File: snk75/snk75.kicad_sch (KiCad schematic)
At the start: 19 parts, among them J1 USB_C_Receptacle_USB2.0, U1 ATmega32U4-AU, Y1 16MHZ

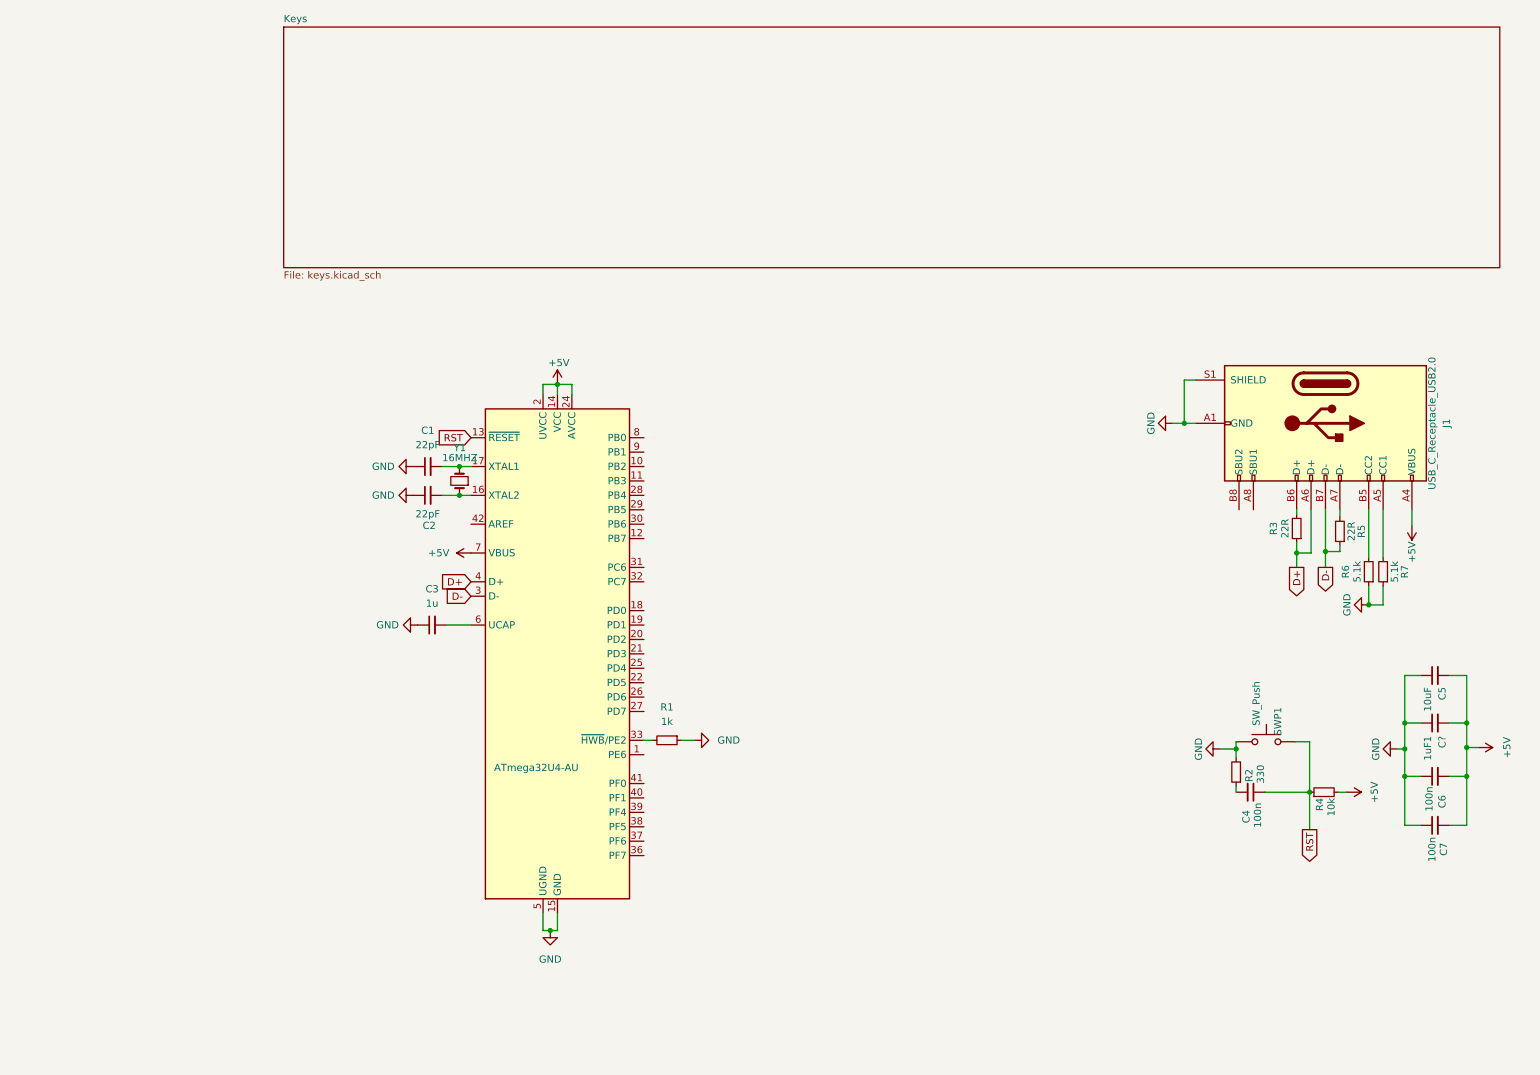
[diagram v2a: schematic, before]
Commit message: Fixed reset
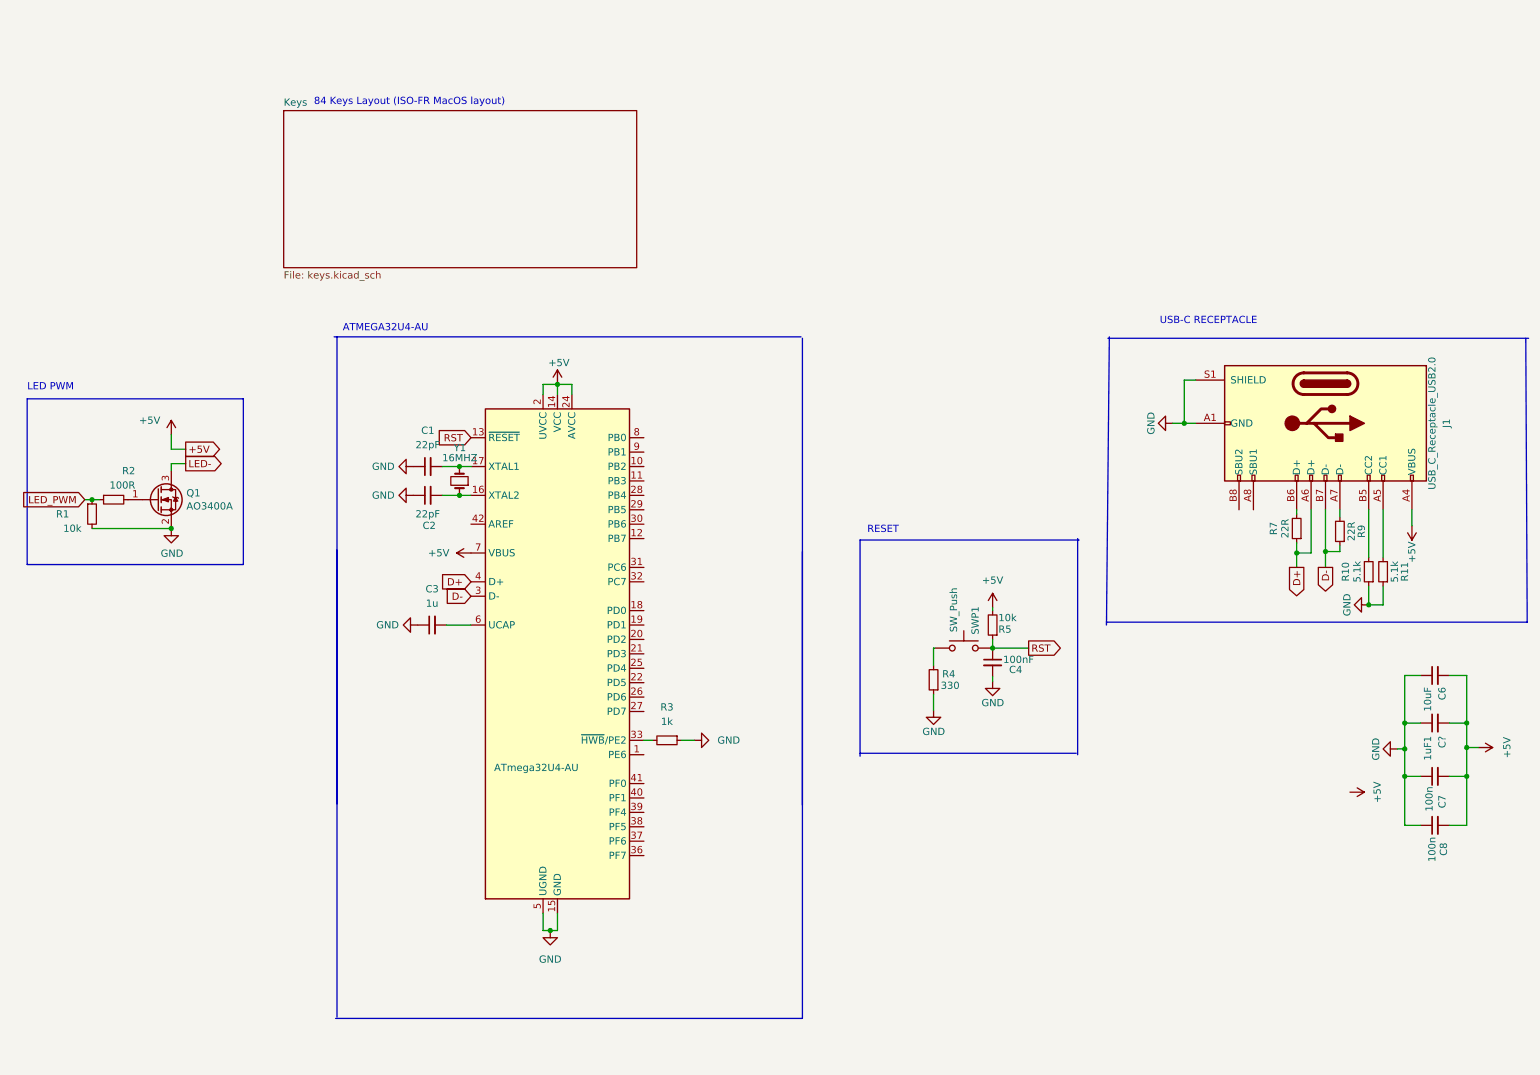
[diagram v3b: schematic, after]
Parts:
- added Q1: AO3400A, Package_TO_SOT_SMD:SOT-23, symbol Device:Q_NMOS_GSD
- added R1: 10k, Resistor_SMD:R_0402_1005Metric, symbol Device:R_Small
- added R5: 10k, Resistor_SMD:R_1206_3216Metric_Pad1.30x1.75mm_HandSolder, symbol Device:R_Small
- C4: value 100n -> 100nF
- R2: value 330 -> 100R; footprint Resistor_SMD:R_1206_3216Metric_Pad1.30x1.75mm_HandSolder -> Resistor_SMD:R_0402_1005Metric; LCSC (none) -> C25076
- R4: value 10k -> 330
- renumbered C5 to C6, C6 to C7, C7 to C8, R6 to R10, R7 to R11, R1 to R3, R3 to R7, R5 to R9
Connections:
- net +5V: now also R5.2; no longer R4.2
- net GND: now also C4.2, R4.1, Q1.2 (S), R1.2; no longer R2.2, SWP1.1
- net RST: now also R5.1; no longer R4.1
- net LED_PWM: now reaches R2.1
- net LED_PWM: now also R1.1; no longer C4.2
- new net: Q1.1 (G), R2.2
- new net: R4.2, SWP1.1
- new net LED-: Q1.3 (D)
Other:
- note added: "84 Keys Layout (ISO-FR MacOS layout)"
- note added: "ATMEGA32U4-AU"
- note added: "LED PWM"
- note added: "RESET"
- note added: "USB-C RECEPTACLE"

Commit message: Fixed label
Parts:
- C6: renamed from 1uF1; value C? -> 1uF
- renumbered C6 to C5, R7 to R6, R9 to R7, R10 to R8, R11 to R9

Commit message: Began routing
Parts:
- removed J1: USB_C_Receptacle_USB2.0, Connector_USB:USB_C_Receptacle_Palconn_UTC16-G, symbol Connector:USB_C_Receptacle_USB2.0
- removed R8, R9: 5.1k, Resistor_SMD:R_1206_3216Metric_Pad1.30x1.75mm_HandSolder, symbol Device:R_Small
- added C10: 100n, Capacitor_SMD:C_0805_2012Metric_Pad1.18x1.45mm_HandSolder, symbol Device:C_Small
- added C9: 1u, Capacitor_SMD:C_0805_2012Metric_Pad1.18x1.45mm_HandSolder, symbol Device:C_Small
- added FB1: FerriteBead_Small, Inductor_SMD:L_0805_2012Metric, symbol Device:FerriteBead_Small
- added J1: TYPE-C-31-M12_13, acheron_Connectors:TYPE-C-31-M-12, symbol acheronSymbols:TYPE-C-31-M12_13
- added U2: USBLC6-2SC6, Package_TO_SOT_SMD:SOT-23-6, symbol Power_Protection:USBLC6-2SC6
- C5: value 10uF -> 10u
- C6: value 1uF -> 1u
- R6, R7: value 22R -> 5.1k
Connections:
- net +5V: now also U1.42 (AREF), C10.2, C9.2
- net D+: now also U2.1 (I/O1); no longer R6.1
- net D-: now also U2.3 (I/O2); no longer R7.1
- net GND: now also R6.1, R7.1, C10.1, C9.1, FB1.1, J1.A1 (GND), J1.B1 (GND), U2.2 (GND)
- net at R7.2: now also J1.A5 (CC1)
- net at R6.2: now also J1.B5 (CC2)
- new net DBUS+: J1.A6 (D+), J1.B6 (D+), U2.6 (I/O1)
- new net DBUS-: J1.A7 (D-), J1.B7 (D-), U2.4 (I/O2)
- new net GNDPWR: FB1.2, J1.S (SHIELD)
- new net VBUS: J1.A4 (VBUS), J1.B4 (VBUS), U2.5 (VBUS)
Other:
- added sheet RGB Underglow (underglow.kicad_sch)
- note added: "USB-C CONNECTOR"
- note added: "USB-C ESD (Suppressor)"
- note removed: "USB-C RECEPTACLE"
- moved on the sheet: C4, C5, C6, C7, C8, Q1, R1, R2, R4, R5, SWP1

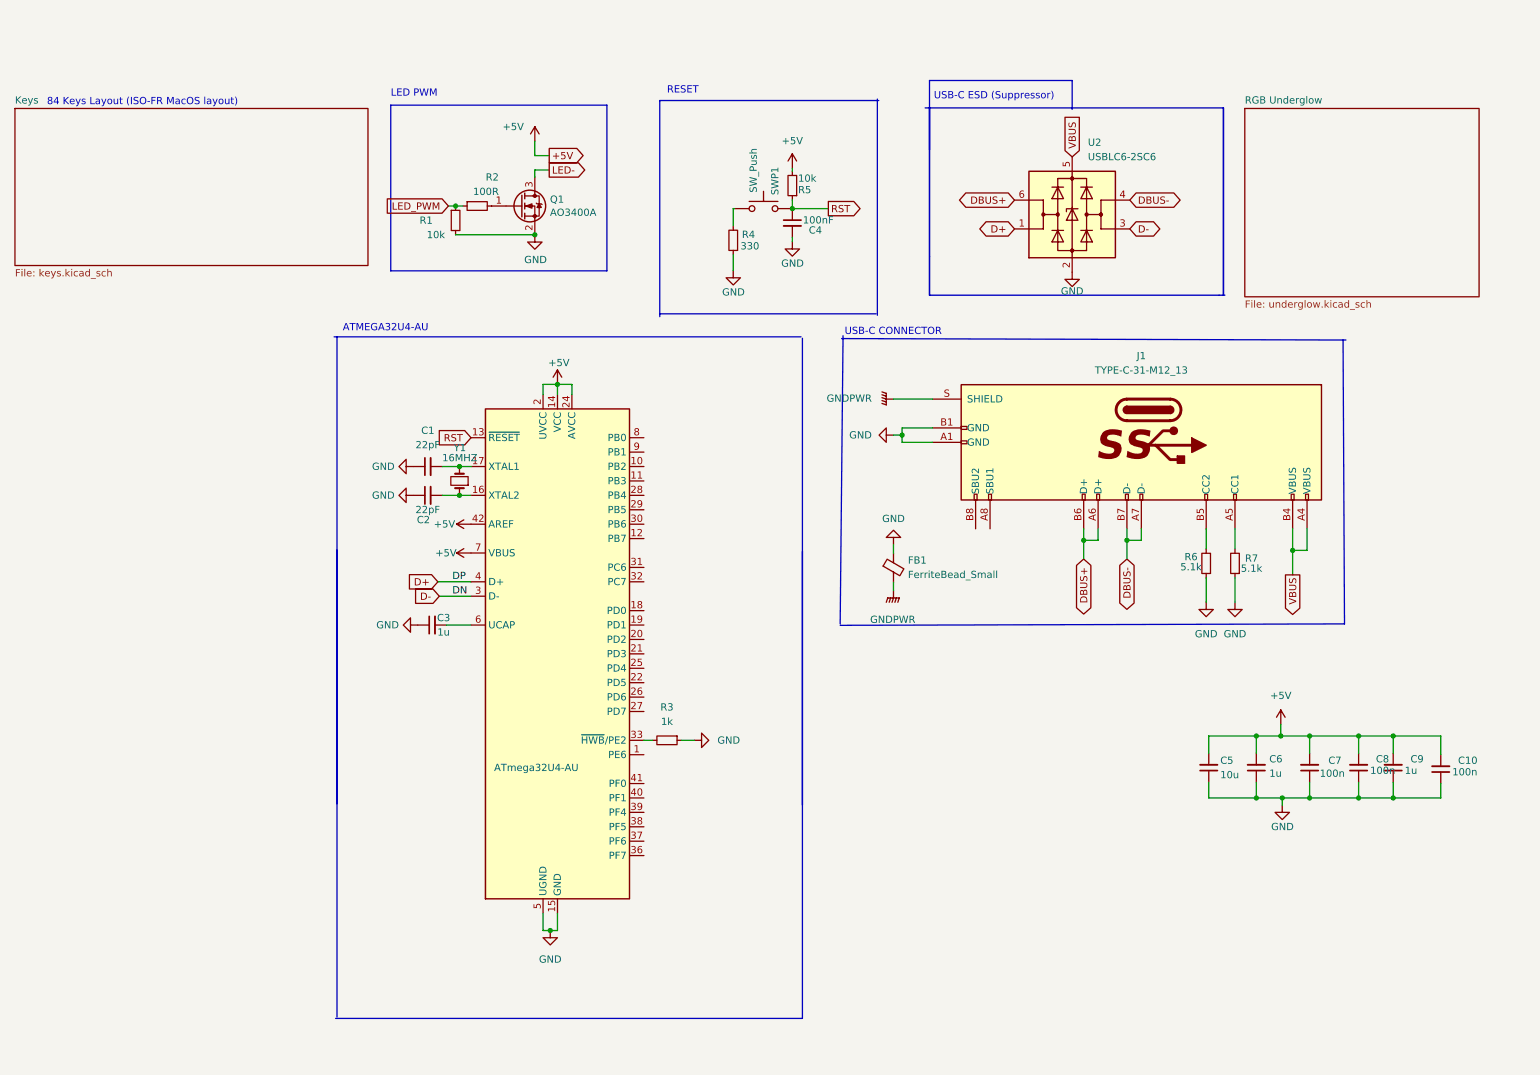
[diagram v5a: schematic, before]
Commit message: Changed MCU for STM32F072C8Tx and wired cols and rows
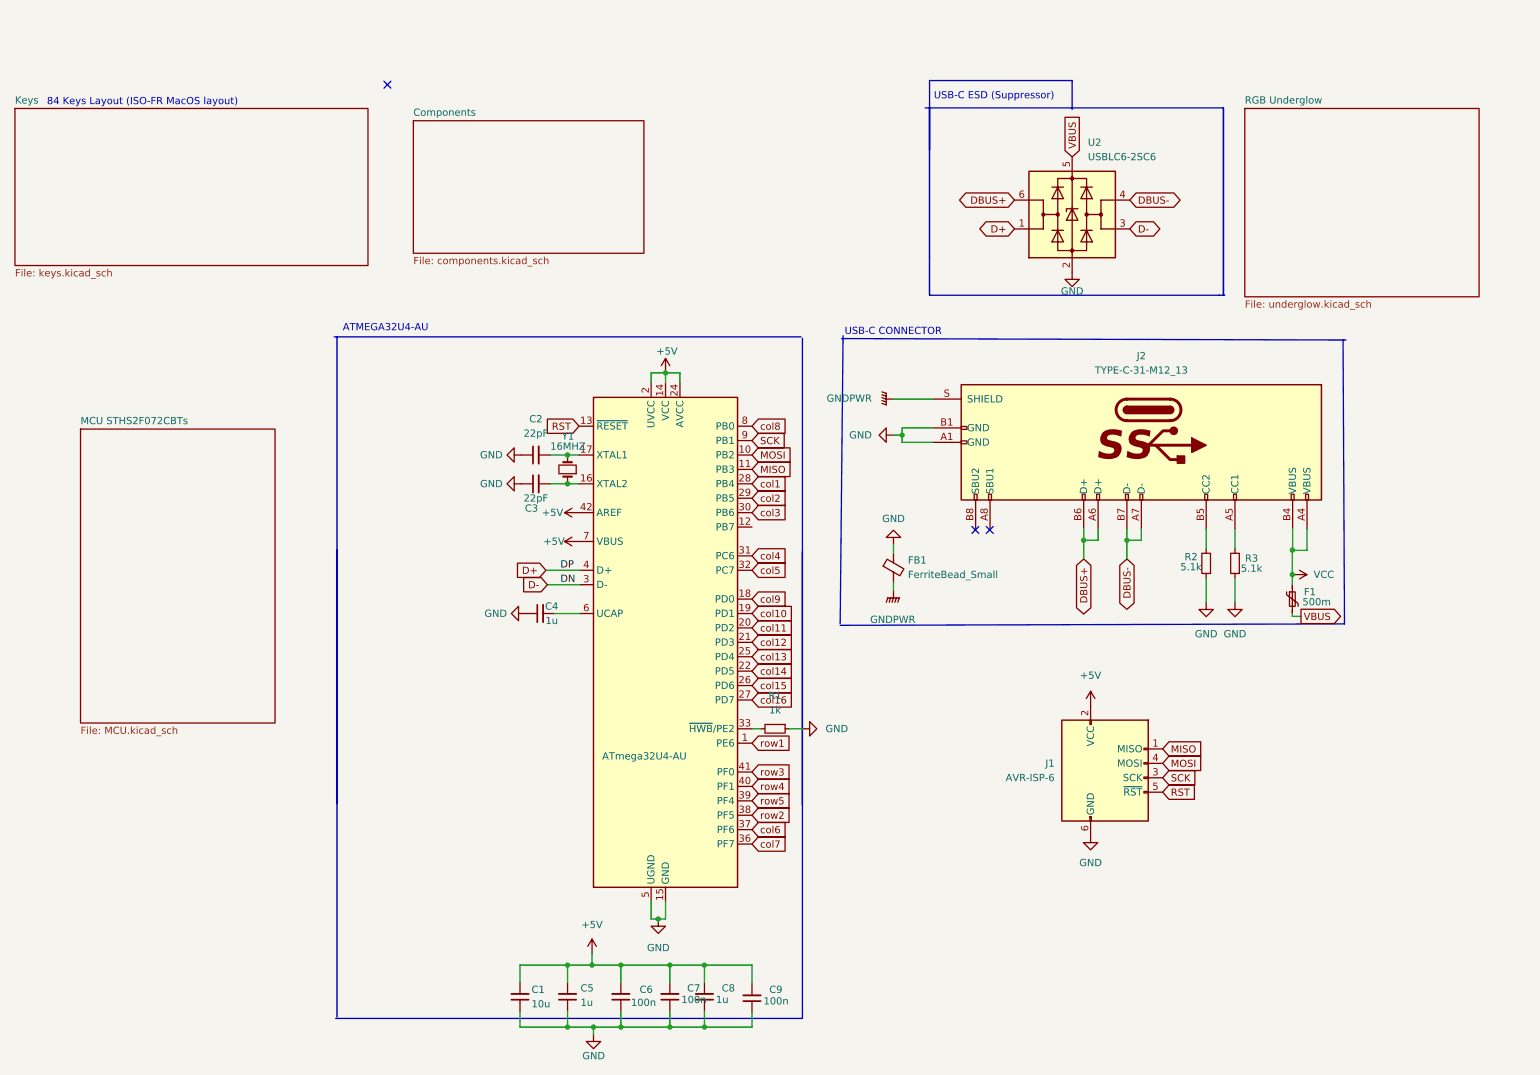
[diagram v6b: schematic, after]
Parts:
- removed C4: 100nF, Capacitor_SMD:C_0805_2012Metric_Pad1.18x1.45mm_HandSolder, symbol Device:C_Small
- removed Q1: AO3400A, Package_TO_SOT_SMD:SOT-23, symbol Device:Q_NMOS_GSD
- removed R1: 10k, Resistor_SMD:R_0402_1005Metric, symbol Device:R_Small
- removed R2: 100R, Resistor_SMD:R_0402_1005Metric, symbol Device:R_Small
- removed R4: 330, Resistor_SMD:R_1206_3216Metric_Pad1.30x1.75mm_HandSolder, symbol Device:R_Small
- removed R5: 10k, Resistor_SMD:R_1206_3216Metric_Pad1.30x1.75mm_HandSolder, symbol Device:R_Small
- removed SWP1: SW_Push, Button_Switch_SMD:SW_MEC_5GSH9, symbol Switch:SW_Push
- added F1: 500m, symbol Device:Polyfuse_Small
- added J1: AVR-ISP-6, symbol Connector:AVR-ISP-6
- C1: renamed from C5; footprint Capacitor_SMD:C_0805_2012Metric_Pad1.18x1.45mm_HandSolder -> Capacitor_SMD:C_0402_1005Metric
- C2: renamed from C1; footprint Capacitor_SMD:C_0805_2012Metric_Pad1.18x1.45mm_HandSolder -> Capacitor_SMD:C_0402_1005Metric
- C3: renamed from C2; footprint Capacitor_SMD:C_0805_2012Metric_Pad1.18x1.45mm_HandSolder -> Capacitor_SMD:C_0402_1005Metric_Pad0.74x0.62mm_HandSolder
- C4: renamed from C3; footprint Capacitor_SMD:C_0805_2012Metric_Pad1.18x1.45mm_HandSolder -> Capacitor_SMD:C_0402_1005Metric_Pad0.74x0.62mm_HandSolder
- C5: renamed from C6; footprint Capacitor_SMD:C_0805_2012Metric_Pad1.18x1.45mm_HandSolder -> Capacitor_SMD:C_0402_1005Metric
- C6: renamed from C7; footprint Capacitor_SMD:C_0805_2012Metric_Pad1.18x1.45mm_HandSolder -> Capacitor_SMD:C_0402_1005Metric
- C7: renamed from C8; footprint Capacitor_SMD:C_0805_2012Metric_Pad1.18x1.45mm_HandSolder -> Capacitor_SMD:C_0402_1005Metric
- C8: renamed from C9; footprint Capacitor_SMD:C_0805_2012Metric_Pad1.18x1.45mm_HandSolder -> Capacitor_SMD:C_0402_1005Metric
- C9: renamed from C10; footprint Capacitor_SMD:C_0805_2012Metric_Pad1.18x1.45mm_HandSolder -> Capacitor_SMD:C_0402_1005Metric
- R1: renamed from R3; footprint Resistor_SMD:R_1206_3216Metric_Pad1.30x1.75mm_HandSolder -> Resistor_SMD:R_0402_1005Metric
- R2: renamed from R6; footprint Resistor_SMD:R_1206_3216Metric_Pad1.30x1.75mm_HandSolder -> Resistor_SMD:R_0402_1005Metric
- R3: renamed from R7; footprint Resistor_SMD:R_1206_3216Metric_Pad1.30x1.75mm_HandSolder -> Resistor_SMD:R_0402_1005Metric
- U2: footprint Package_TO_SOT_SMD:SOT-23-6 -> acheron_Components:SOT-23-6
- renumbered J1 to J2
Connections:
- net +5V: now also J1.2 (VCC)
- net GND: now also J1.6 (GND)
- net RST: now also J1.5 (~{RST})
- net VBUS: now also F1.2; no longer J2.A4 (VBUS), J2.B4 (VBUS)
- net row1: now reaches U1.1 (PE6)
- net MOSI: now reaches U1.10 (PB2)
- net MOSI: now also J1.4 (MOSI)
- net MISO: now reaches U1.11 (PB3)
- net MISO: now also J1.1 (MISO)
- net col9: now reaches U1.18 (PD0)
- net col10: now reaches U1.19 (PD1)
- net col11: now reaches U1.20 (PD2)
- net col12: now reaches U1.21 (PD3)
- net col14: now reaches U1.22 (PD5)
- net col13: now reaches U1.25 (PD4)
- net col15: now reaches U1.26 (PD6)
- net col16: now reaches U1.27 (PD7)
- net col1: now reaches U1.28 (PB4)
- net col2: now reaches U1.29 (PB5)
- net col3: now reaches U1.30 (PB6)
- net col4: now reaches U1.31 (PC6)
- net col5: now reaches U1.32 (PC7)
- net col7: now reaches U1.36 (PF7)
- net col6: now reaches U1.37 (PF6)
- net row2: now reaches U1.38 (PF5)
- net row5: now reaches U1.39 (PF4)
- net row4: now reaches U1.40 (PF1)
- net row3: now reaches U1.41 (PF0)
- net col8: now reaches U1.8 (PB0)
- net SCK: now reaches U1.9 (PB1)
- net SCK: now also J1.3 (SCK)
- new net: J2.A4 (VBUS), J2.B4 (VBUS)
- new net VCC: F1.1
- no-connect marks 0 -> 3
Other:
- added sheet Components (components.kicad_sch)
- added sheet MCU STHS2F072CBTs (MCU.kicad_sch)
- note removed: "LED PWM"
- note removed: "RESET"
- moved on the sheet: C1, C2, C3, C4, C5, C6, C7, C8, C9, R1, Y1
